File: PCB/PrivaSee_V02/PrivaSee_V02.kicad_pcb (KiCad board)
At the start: 4 copper layers, 69.8 x 90 mm, 23 parts, among them J2 Batt_Solder_Point, SW1 (Generic toggle state switch), U2 LM358, U3 254, U4 DFR0568, U5 LM358, U6 ESP32-C5-DevKitC-1

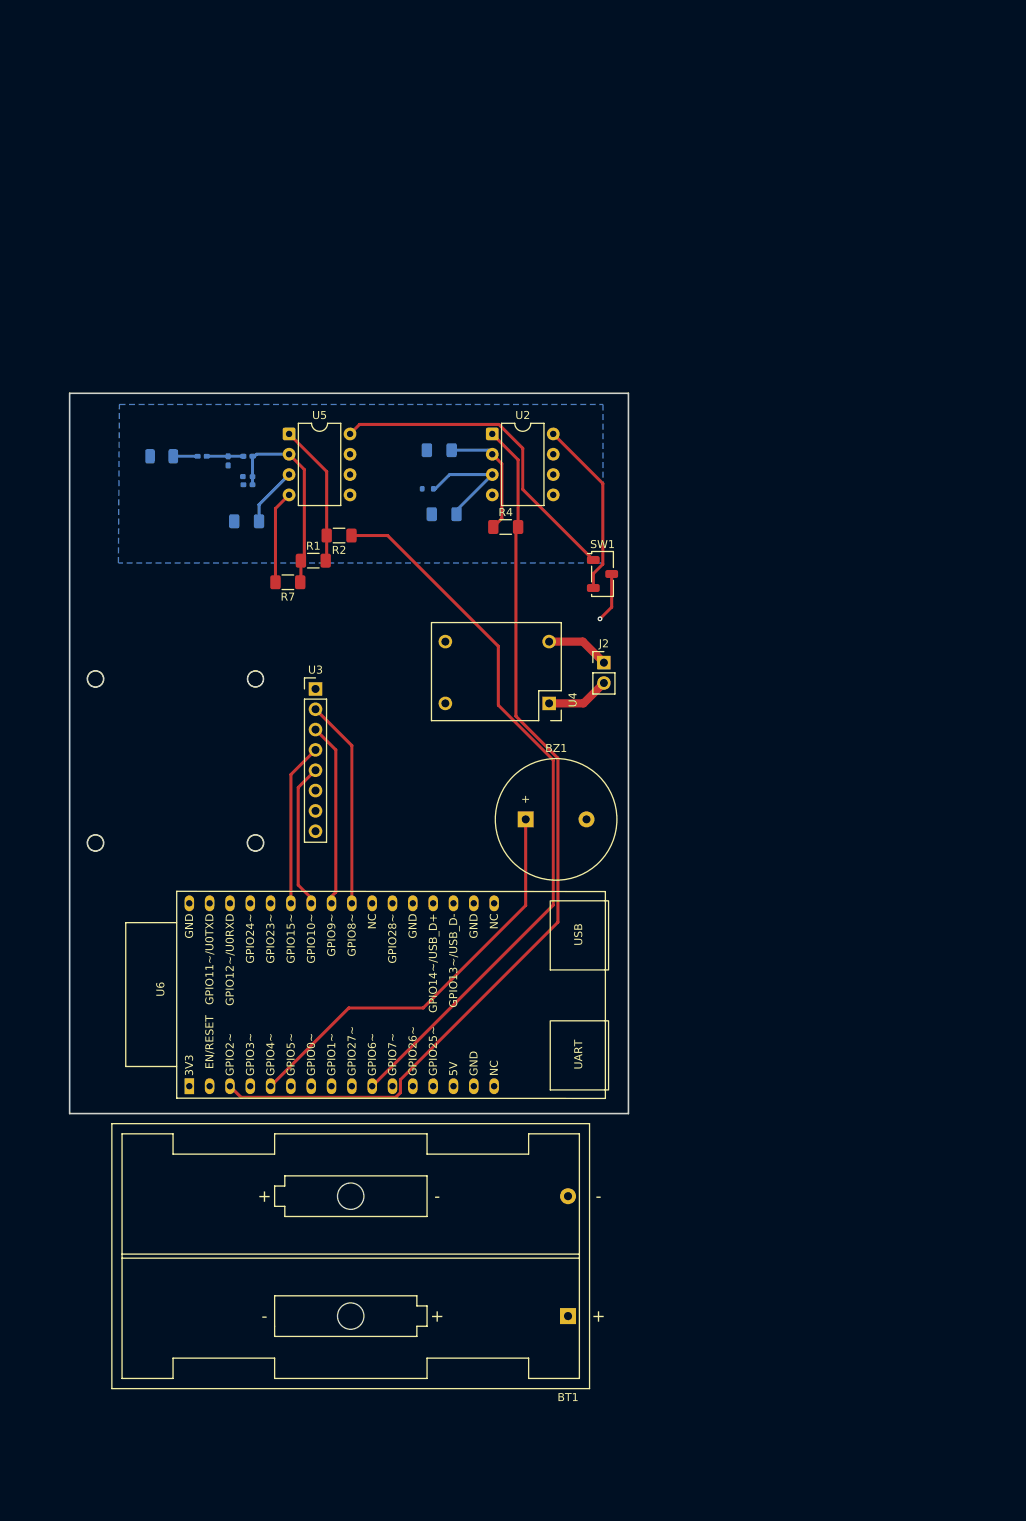
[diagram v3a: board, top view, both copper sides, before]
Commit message: PCB Updates
Added a screen, updated the connector for the SMA through hole component, and rearranged to fit
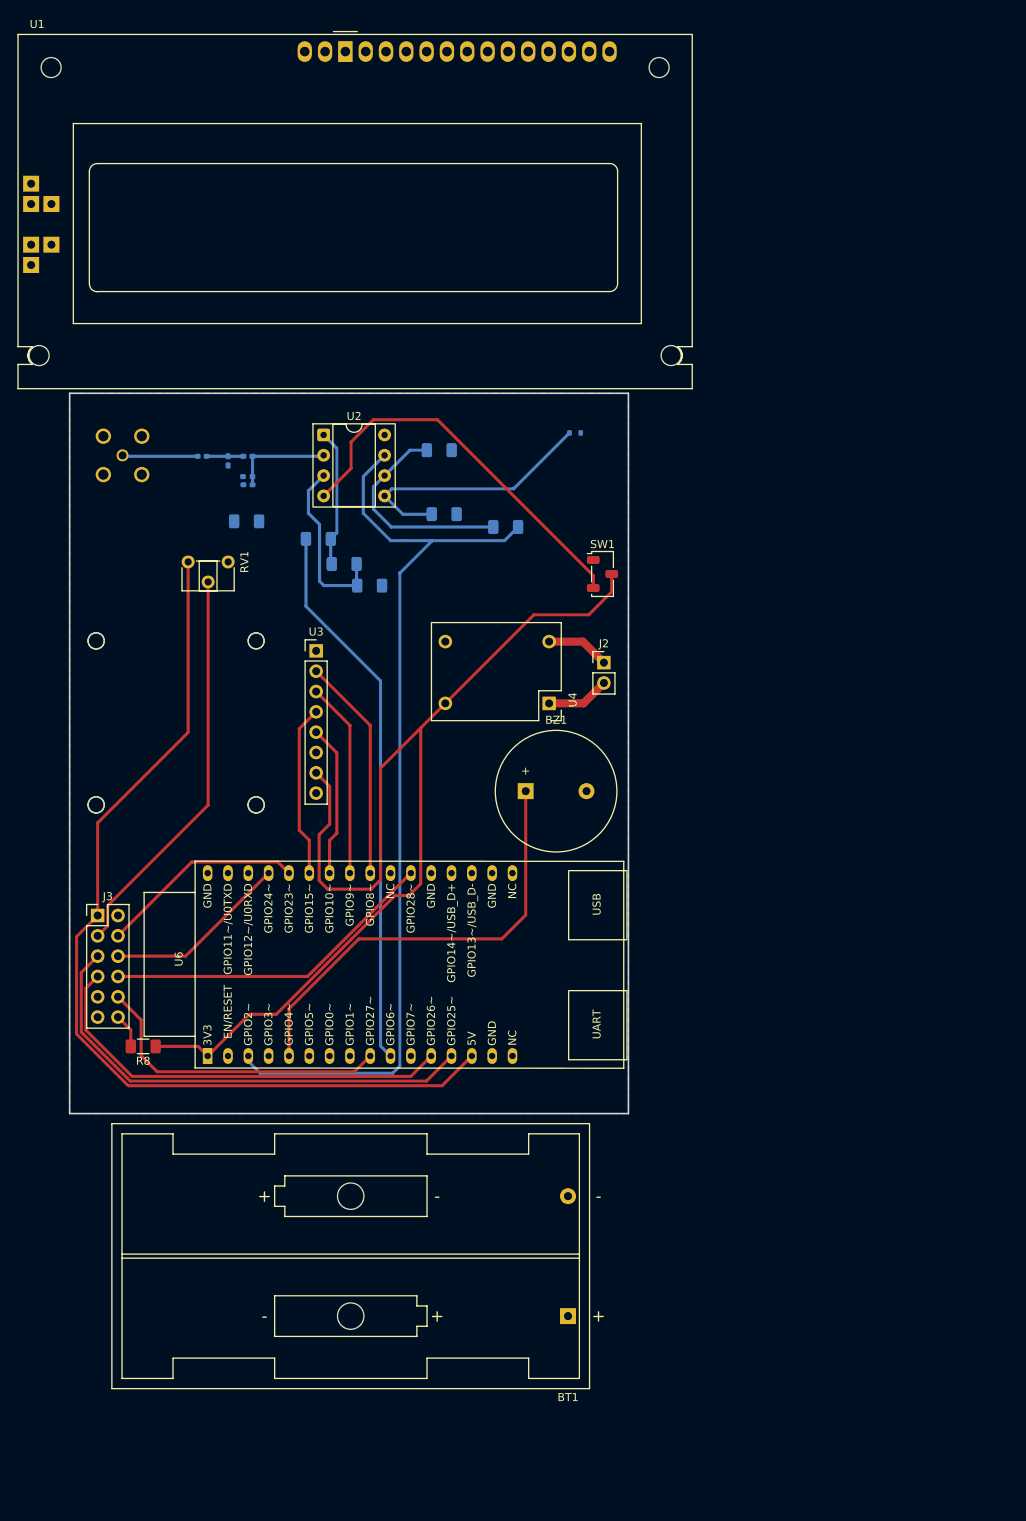
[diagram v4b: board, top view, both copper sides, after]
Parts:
- removed AE1: SMA_Conn, RF_Antenna:Johanson_2450AT18x100_2400-2500Mhz
- removed U5: LM358, Package_DIP:DIP-8_W7.62mm
- added J1: SMA_CONNECTOR, SMA_CONNECTOR:LPRS_SMA_CONNECTOR, B.Cu at (72.7, 29.4)
- added J3: Conn_02x06_Odd_Even, Connector_PinHeader_2.54mm:PinHeader_2x06_P2.54mm_Vertical, F.Cu at (69.5, 86.9)
- added R8: 100 ohm, Resistor_SMD:R_1206_3216Metric_Pad1.30x1.75mm_HandSolder, F.Cu at (75.2, 103.2)
- added RV1: 10k, Potentiometer_THT:Potentiometer_ACP_CA6-H2,5_Horizontal, F.Cu at (85.9, 42.7)
- added U1: RC1602A, Display:RC1602A, F.Cu at (100.5, -21.1)
- R1, R2, R4, R7: moved to B.Cu
- U2: footprint Package_DIP:DIP-8_W7.62mm -> Package_DIP:DIP-8_W7.62mm_Socket
- moved U2 21.1 mm to (97.8, 26.8)
- moved D3 19.7 mm to (129.2, 26.5), turned to 0 degrees
- moved R7 10.2 mm to (103.5, 45.6), turned to 0 degrees
- moved U3 4.76 mm to (96.9, 53.8)
- moved U6 4.42 mm to (83.3, 104.5)
- moved R1 3.88 mm to (100.4, 42.9), turned to 180 degrees
- moved BZ1 3.53 mm to (123.0, 71.3)
- moved R2 2.62 mm to (97.1, 39.8), turned to 0 degrees
- turned R3 to 180 degrees
- turned R5 to 180 degrees
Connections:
- R1 pad 1: Net-(U5A--) -> Net-(U2A-+)
- R3 pad 2: Net-(U2A--) -> Net-(U2B--)
- R4 pad 1: Net-(U2A--) -> Net-(U2B--)
- R7 pad 1: Net-(U5A--) -> Net-(U2A-+)
- SW1 pad 1: Net-(SW1-C) -> unconnected-(SW1-C-Pad1)
- U2 pad 1: Net-(U6-GPIO2/MTMS) -> Net-(R1-Pad2)
- U2 pad 2: Net-(U2A--) -> Net-(D2-K)
- U2 pad 3: Net-(D3-K) -> Net-(U2A-+)
- U2 pad 4: GND -> Net-(SW1-A)
- U2 pad 5: (no net) -> Net-(D3-K)
- U2 pad 6: (no net) -> Net-(U2B--)
- U2 pad 7: (no net) -> Net-(U6-GPIO2/MTMS)
- U2 pad 8: Net-(SW1-A) -> GND
- U6 pad 12: unconnected-(U6-GPIO26-Pad12) -> LCD_DB7
- U6 pad 13: unconnected-(U6-GPIO25-Pad13) -> LCD_DB6
- U6 pad 14: unconnected-(U6-5V-Pad14) -> 5V
- U6 pad 22: unconnected-(U6-GPIO28-Pad22) -> LCD_RS
- U6 pad 28: unconnected-(U6-GPIO23-Pad28) -> LCD_DB4
- U6 pad 29: unconnected-(U6-GPIO24-Pad29) -> LCD_DB5
- U6 pad 9: unconnected-(U6-GPIO27-Pad9) -> LCD_E
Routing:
- net /3V3: track 9.04 -> 139.6 mm, vias 1 -> 0
- net 5V: track 0.00 -> 118.4 mm
- net LCD_DB6: track 0.00 -> 60.5 mm
- net LCD_DB7: track 0.00 -> 53.9 mm
- net VVAR: track 0.00 -> 50.0 mm
- net LCD_RS: track 0.00 -> 42.0 mm
- net Net-(SW1-C): track 40.9 -> 0.00 mm
- net LCD_E: track 0.00 -> 38.8 mm
- net Net-(U2B--): track 0.00 -> 27.3 mm
- net Net-(SW1-A): track 22.3 -> 49.2 mm
- net LCD_DB4: track 0.00 -> 25.8 mm
- net LCD_DB5: track 0.00 -> 23.1 mm
- net Net-(U6-GPIO6): track 91.3 -> 69.0 mm
- net Net-(U2A-+): track 0.00 -> 22.1 mm
- net Net-(D3-K): track 15.0 -> 33.2 mm
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- removed copper zone on In1.Cu, net /3V3
- removed copper zone on In2.Cu, net GND
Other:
- copper layers 4 -> 2

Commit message: RF parts placed
Swapped out the schematic with my components
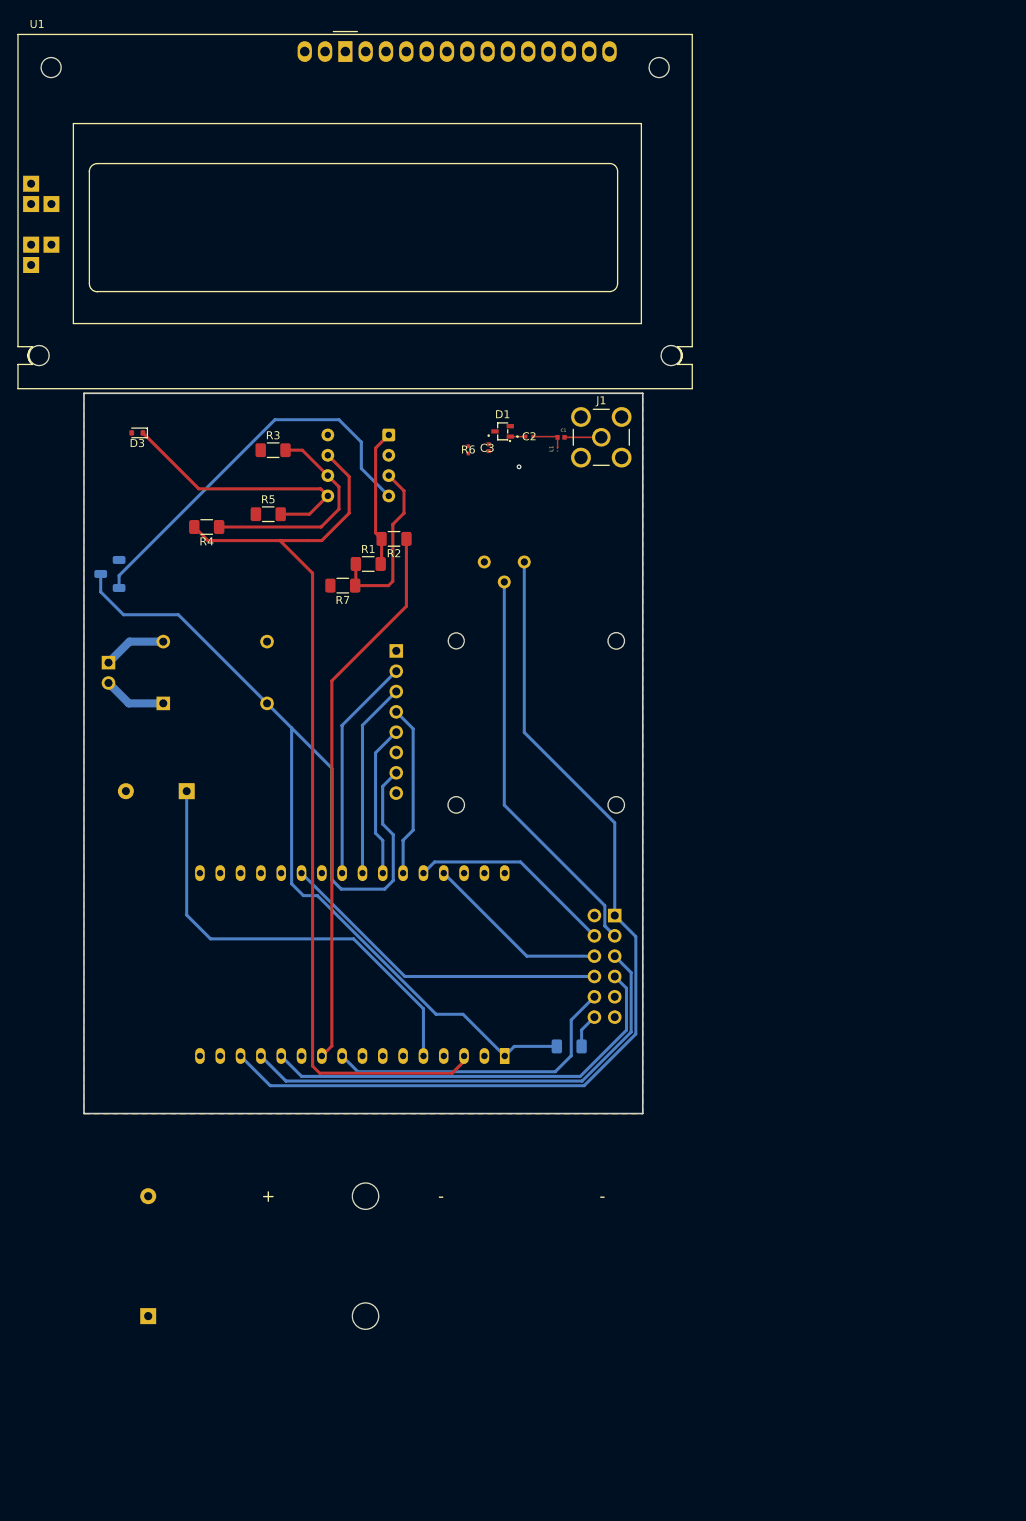
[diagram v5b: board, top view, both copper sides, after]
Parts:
- removed D2: Schottky, Diode_SMD:D_0402_1005Metric_Pad0.77x0.64mm_HandSolder
- removed the R1 at (88.2, 37.6)
- added C3: GJM1555C1H220FB01D, Snapeda:CAP_GJM1555C1H220FB01D_MUR-L, F.Cu at (118.4, 28.4)
- added L1: LQP02HQ9N1H02E, Snapeda:IND_LQP02HQ9N1H02E, F.Cu at (127.0, 28.6)
- BT1, BZ1, J2, J3, R8, RV1, SW1, U2, U3, U4, U6: moved to B.Cu
- C1: value 4.7pF -> GJM1555C1HR22BB01D; footprint Capacitor_SMD:C_0402_1005Metric_Pad0.74x0.62mm_HandSolder -> Snapeda:CAPC1005X55N; moved to F.Cu
- C2: value 22pF -> GJM1555C1H4R7CB01D; footprint Capacitor_SMD:C_0402_1005Metric_Pad0.74x0.62mm_HandSolder -> Snapeda:G-155_MUR-L; moved to F.Cu
- D1: value Schottky -> BAT1504WH6327XTSA1; footprint Diode_SMD:D_0402_1005Metric_Pad0.77x0.64mm_HandSolder -> JLCImport:BAT1504WH6327XTSA1; moved to F.Cu
- D3, R2, R3, R4, R5, R7: moved to F.Cu
- J1: value SMA_CONNECTOR -> RFPC-SMA27-F; footprint SMA_CONNECTOR:LPRS_SMA_CONNECTOR -> Snapeda:GRADCONN_RFPC-SMA27-F; moved to F.Cu
- R1: value 100 -> 200; moved to F.Cu
- R6: value 10k -> RT0402BRE07100KL; footprint Resistor_SMD:R_0402_1005Metric_Pad0.72x0.64mm_HandSolder -> Snapeda:RC0402N_YAG-L; moved to F.Cu
- moved J3 64.6 mm to (134.2, 86.9), turned to 180 degrees
- moved J2 61.9 mm to (70.9, 55.3), turned to 180 degrees
- moved SW1 61.6 mm to (71.1, 44.2), turned to 180 degrees
- moved J1 59.9 mm to (132.5, 27.1), turned to 90 degrees
- moved D3 54.7 mm to (74.5, 26.5), turned to 180 degrees
- moved R8 53.3 mm to (128.5, 103.2), turned to 0 degrees
- moved BT1 52.5 mm to (75.9, 136.9), turned to 0 degrees
- moved U4 48.6 mm to (77.6, 61.2)
- moved C1 44.9 mm to (127.5, 27.1), turned to 0 degrees
- moved BZ1 42.4 mm to (80.7, 71.3), turned to 180 degrees
- moved R4 37.4 mm to (83.2, 38.3), turned to 180 degrees
- moved U6 37.1 mm to (120.4, 104.5)
- moved C2 35.7 mm to (123.5, 27.0)
- moved D1 34.5 mm to (120.2, 26.4), turned to 0 degrees
- moved RV1 32.0 mm to (117.9, 42.7)
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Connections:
- C1 pad 1: Net-(D1-K) -> Net-(C1-Pad1)
- C2 pad 1: GND -> Net-(D1-A)
- C2 pad 2: Net-(D2-K) -> Net-(C1-Pad1)
- D1 pad 1: Net-(D1-K) -> Net-(D1-A)
- R6 pad 1: Net-(D2-K) -> GND
- R6 pad 2: GND -> Net-(D1-C/A)
- U2 pad 2: Net-(D2-K) -> Net-(D1-C/A)
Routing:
- net Net-(D2-K): track 12.5 -> 0.00 mm
- net Net-(C1-Pad2): track 9.43 -> 4.60 mm
- net Net-(D1-K): track 4.58 -> 0.00 mm
- net Net-(C1-Pad1): track 0.00 -> 4.44 mm
- net Net-(D1-A): track 0.00 -> 1.94 mm
- net (no net): vias 0 -> 1
- added copper zone on F.Cu, net GND
- removed copper zone on B.Cu, net GND

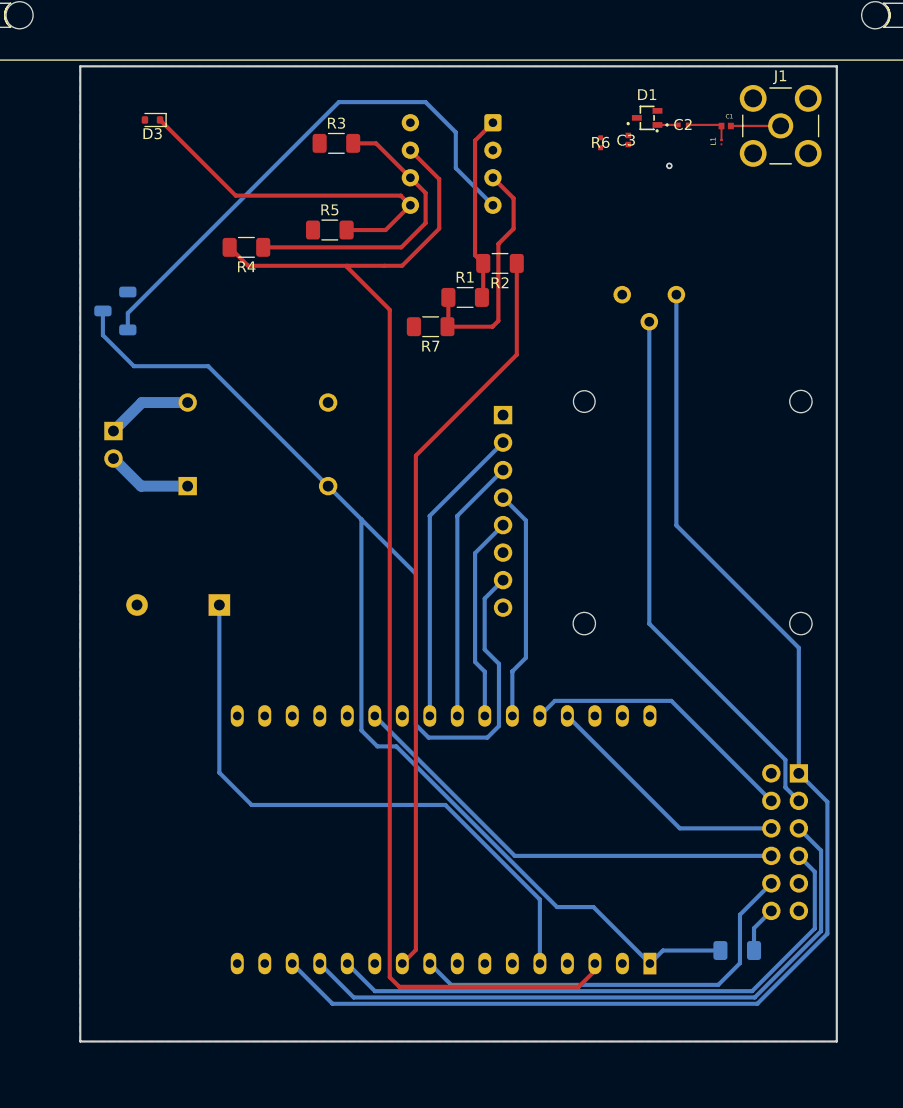
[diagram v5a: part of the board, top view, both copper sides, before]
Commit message: Flipped PCB
Flipped the PCB over and unlocked from Bryson's PC
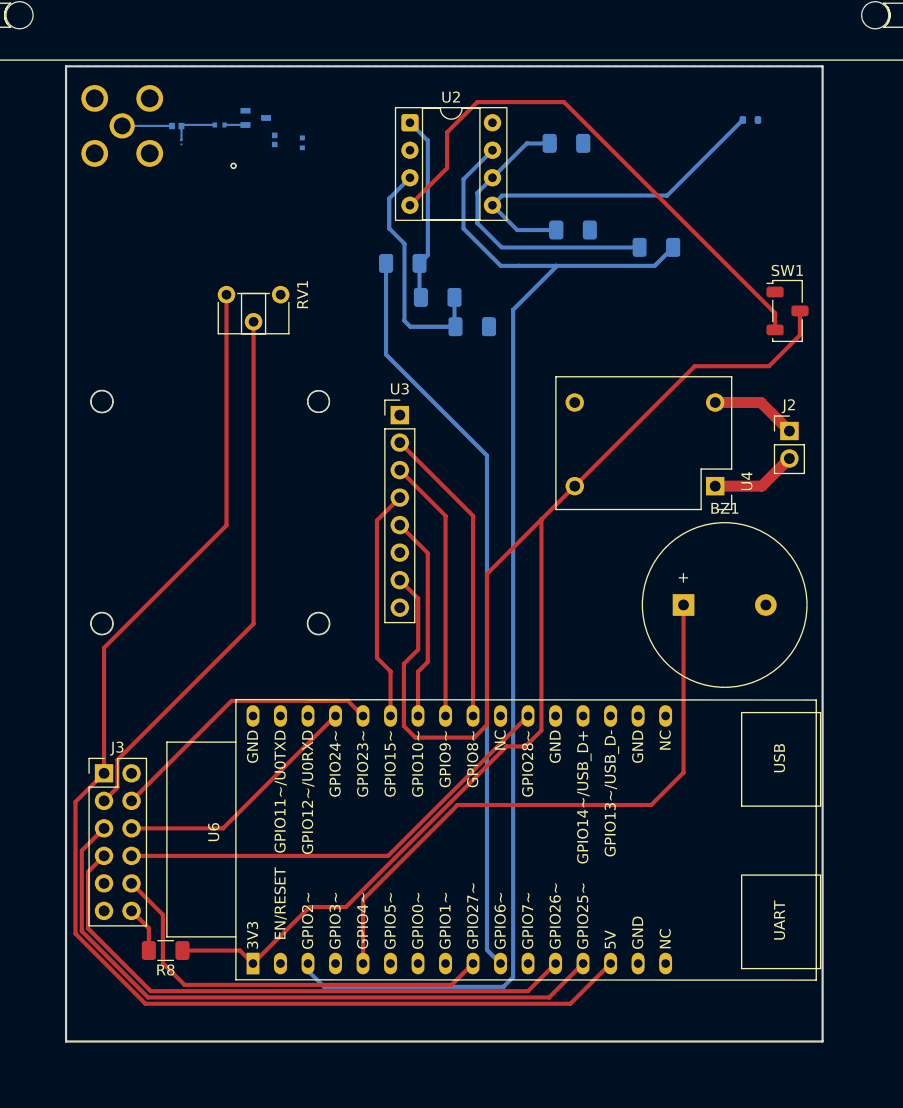
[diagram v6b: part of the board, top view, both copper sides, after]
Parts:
- BZ1, J2, J3, R8, RV1, SW1, U2, U3, U4, U6: moved to F.Cu
- C1, C2, C3, D1, D3, J1, L1, R1, R2, R3, R4, R5, R6, R7: moved to B.Cu
- moved J3 64.2 mm to (70.0, 86.9), turned to 0 degrees
- moved J2 62.4 mm to (133.3, 55.3), turned to 0 degrees
- moved SW1 62.1 mm to (133.1, 44.2), turned to 0 degrees
- moved J1 60.8 mm to (71.7, 27.1)
- moved D3 55.2 mm to (129.7, 26.5), turned to 0 degrees
- moved R8 52.8 mm to (75.7, 103.2), turned to 180 degrees
- moved C1 50.7 mm to (76.7, 27.1), turned to 180 degrees
- moved L1 49.9 mm to (77.2, 28.6)
- moved U4 49.1 mm to (126.6, 61.2)
- moved BZ1 42.9 mm to (123.5, 71.3), turned to 0 degrees
- moved C2 42.8 mm to (80.7, 27.0), turned to 180 degrees
- moved R4 37.9 mm to (121.0, 38.3), turned to 0 degrees
- moved U6 36.6 mm to (83.8, 104.5)
- moved D1 36.1 mm to (84.0, 26.4), turned to 180 degrees
- moved C3 32.6 mm to (85.8, 28.4)
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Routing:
- added copper zone on B.Cu, net GND
- removed copper zone on F.Cu, net GND
